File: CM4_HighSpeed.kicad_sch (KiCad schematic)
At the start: 14 parts, among them J12 THD-02-R, J13 1-2199119-5, J14 USB_A, J15 USB_OTG, J16 Conn_01x02, J2 SS-52400-004, J5 690-019-298-412, U11 TPD4EUSB30, U13 RT9742SNGV

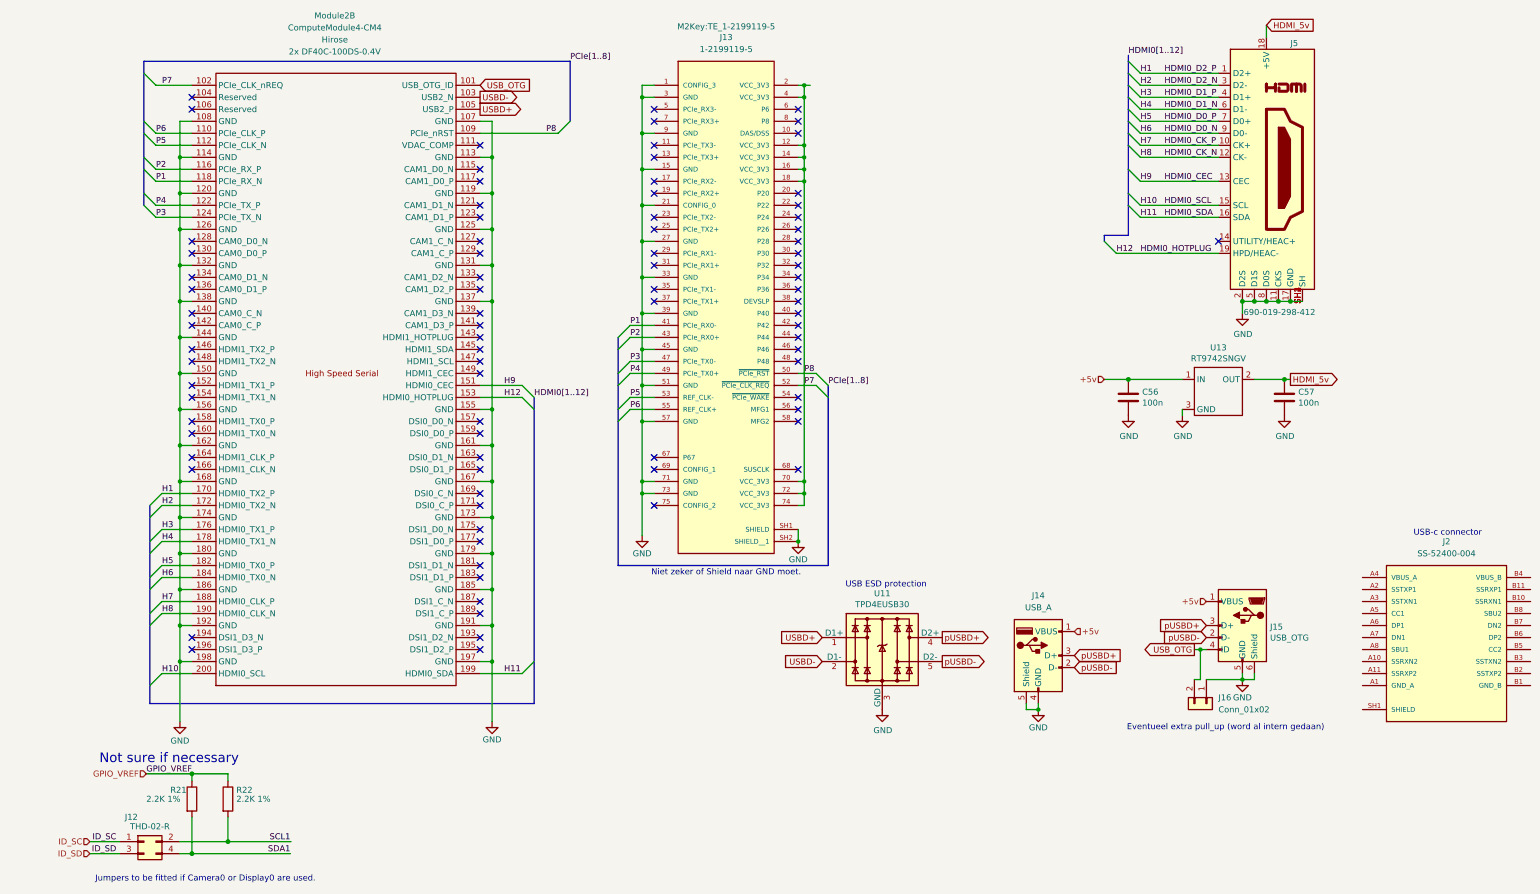
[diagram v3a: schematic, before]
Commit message: Added 3d-models, esd protection, cleaned up and made small start with pcb
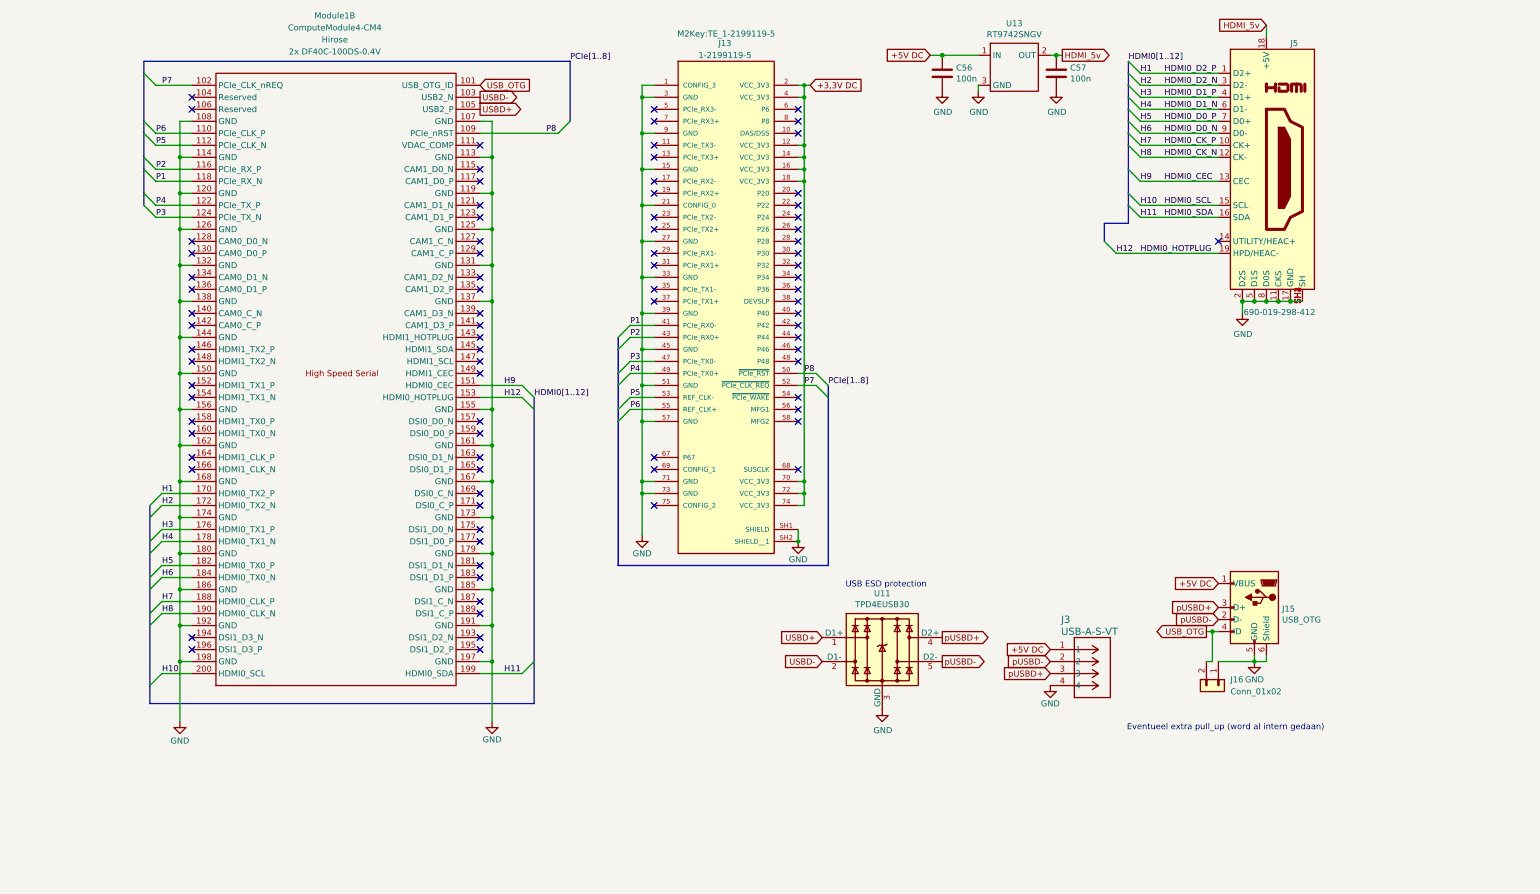
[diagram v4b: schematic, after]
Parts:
- removed J12: THD-02-R, Connector_PinHeader_2.54mm:PinHeader_2x02_P2.54mm_Vertical, symbol Connector_Generic:Conn_02x02_Odd_Even
- removed J14: USB_A, Connector_USB:USB_A_Receptacle_XKB_U231-091N-4BLRA00-S, symbol Connector:USB_A
- removed J2: SS-52400-004, SS-52400-004:STEWART_SS-52400-004 (USB-C), symbol SS-52400-004:SS-52400-004
- removed R21, R22: 2.2K 1%, Resistor_SMD:R_0402_1005Metric, symbol Device:R
- added J3: USB-A-S-VT, USB-A-S-VT:CONN_USB-A-S-VT_ADM, symbol USB-A-S-VT:USB-A-S-VT
- C56, C57: footprint Capacitor_SMD:C_0402_1005Metric -> Capacitor_SMD:C_0603_1608Metric
- J16: footprint (none) -> Connector_PinHeader_2.54mm:PinHeader_1x02_P2.54mm_Vertical
- renumbered Module2 to Module1
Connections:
- net GND: now also J3.4
- net pUSBD+: now also J3.3
- net pUSBD-: now also J3.2
- net +5v renamed +5V DC
- net +5V DC: now also J3.1
- net P7 renamed +3,3V DC
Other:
- note removed: "Jumpers to be fitted if Camera0 or Display0 are used."
- note removed: "Niet zeker of Shield naar GND moet."
- note removed: "Not sure if necessary"
- note removed: "USB-c connector"
- moved on the sheet: C56, C57, J15, J16, U13

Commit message: Adjusted the PCB design, changed footprints to 0402 (temp)
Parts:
- C56, C57: footprint Capacitor_SMD:C_0603_1608Metric -> Capacitor_SMD:C_0402_1005Metric_Pad0.74x0.62mm_HandSolder
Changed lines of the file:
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@@
 			)
 		)
-		(property "Footprint" "Capacitor_SMD:C_0603_1608Metric"
+		(property "Footprint" "Capacitor_SMD:C_0402_1005Metric_Pad0.74x0.62mm_HandSolder"
 			(at 225.7552 29.21 0)
 			(effects
@@
 			)
 		)
-		(property "Footprint" "Capacitor_SMD:C_0603_1608Metric"
+		(property "Footprint" "Capacitor_SMD:C_0402_1005Metric_Pad0.74x0.62mm_HandSolder"
 			(at 201.6252 29.21 0)
 			(effects

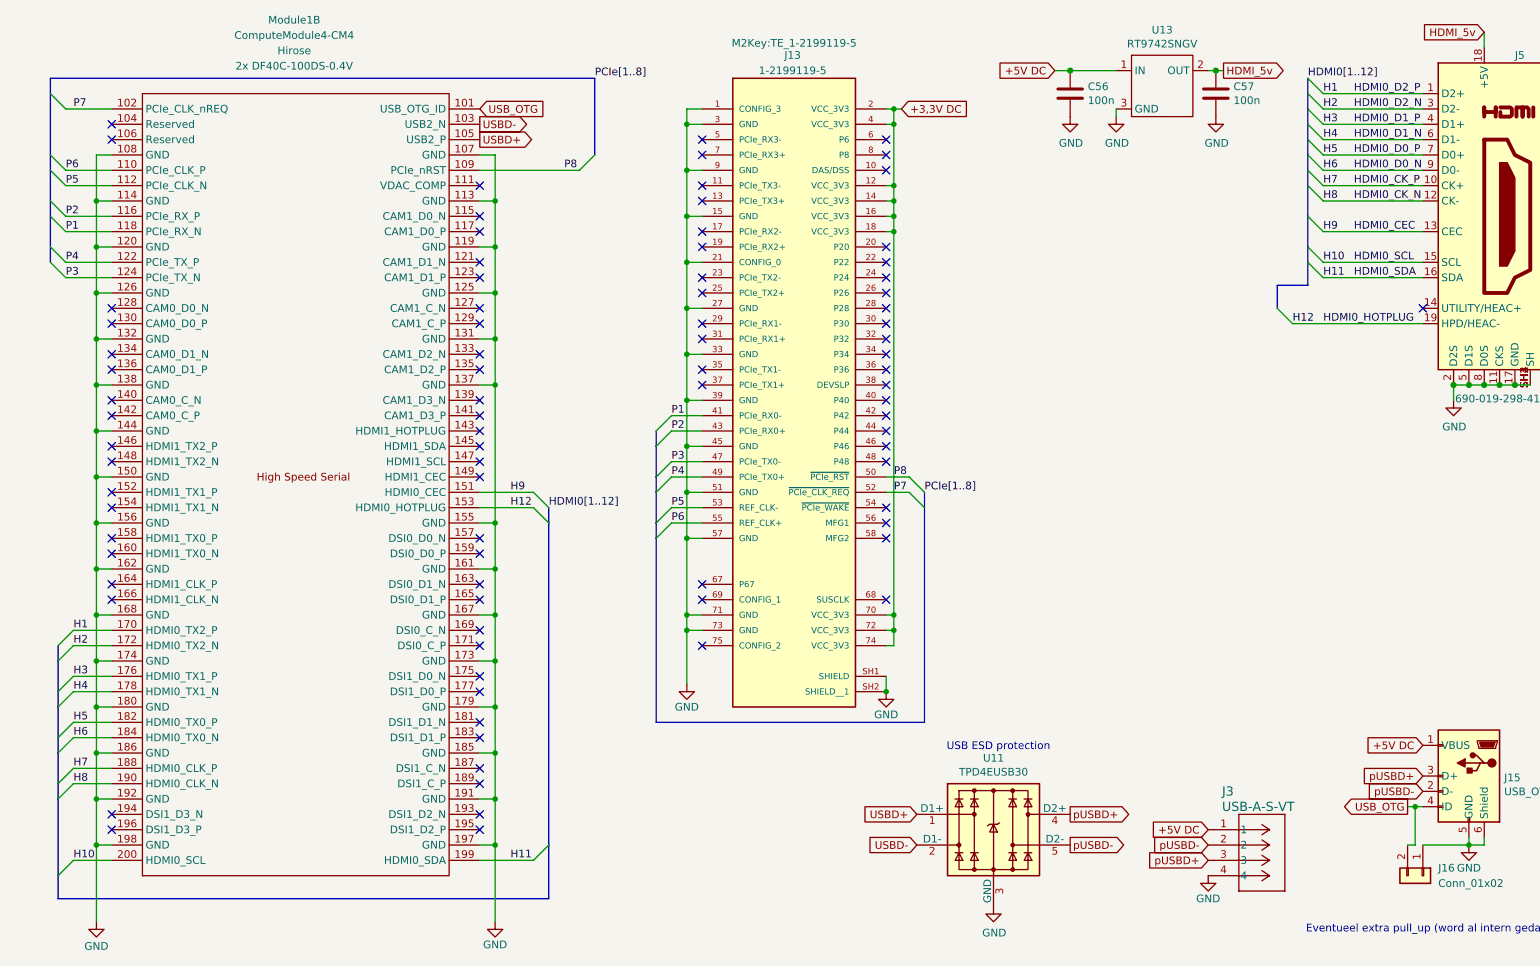
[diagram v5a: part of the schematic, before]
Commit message: Adjusted netclasses to route differential pairs for PCIe and HDMI. And used JLCPCB to adjust trace width for those
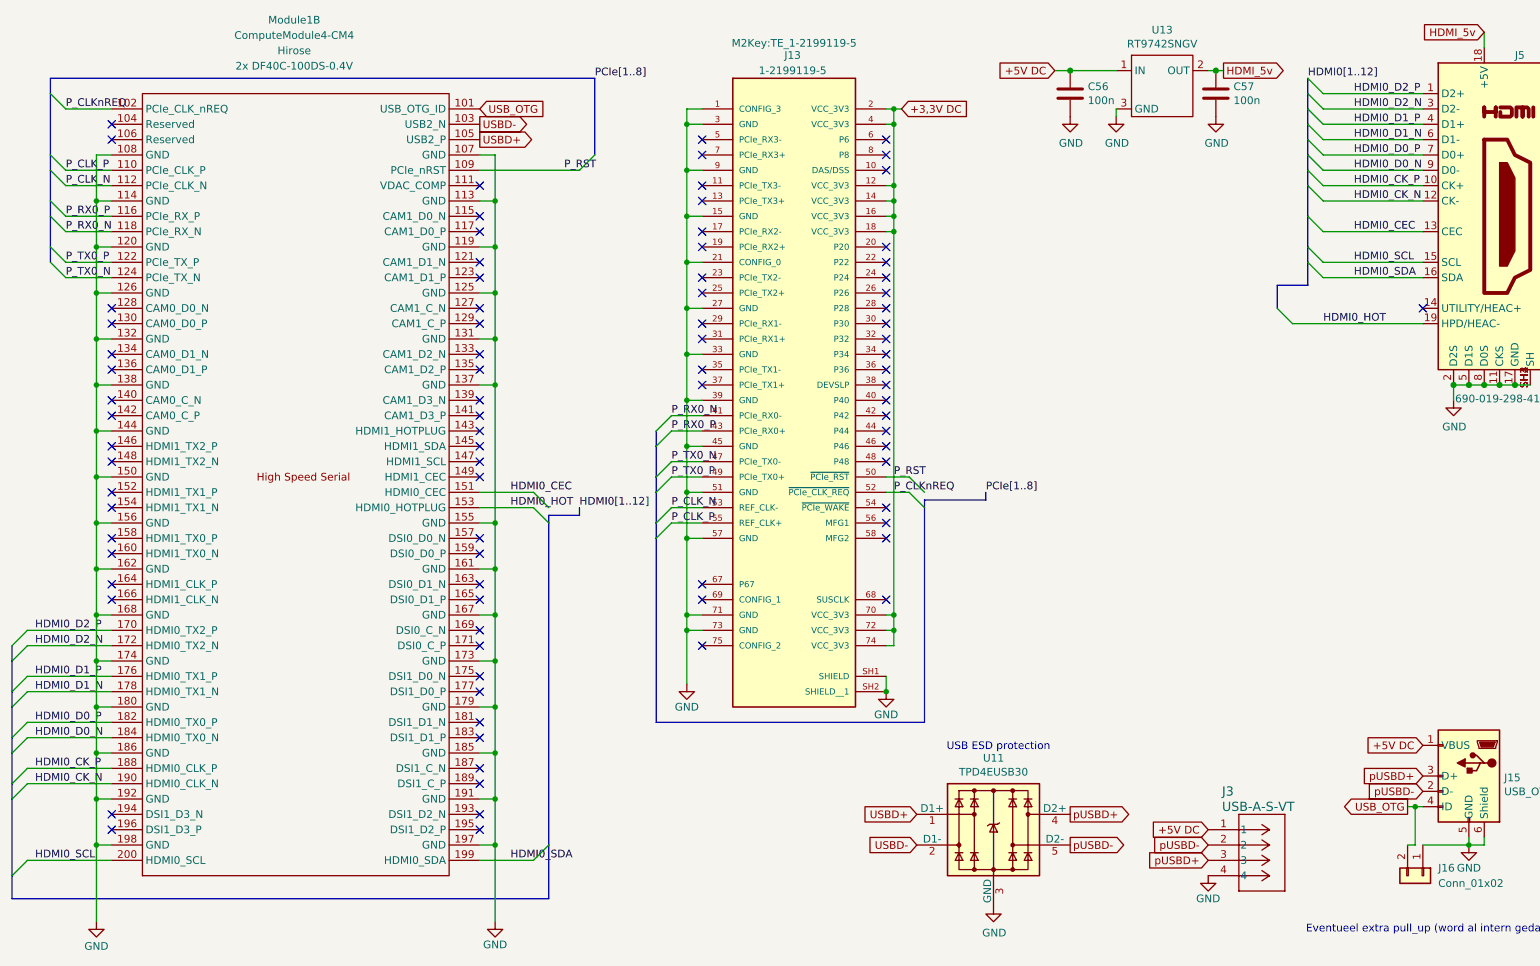
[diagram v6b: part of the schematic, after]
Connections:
- net H1 renamed HDMI0_D2_P
- net H10 renamed HDMI0_SCL
- net H11 renamed HDMI0_SDA
- net H12 renamed HDMI0_HOT
- net H2 renamed HDMI0_D2_N
- net H3 renamed HDMI0_D1_P
- net H4 renamed HDMI0_D1_N
- net H5 renamed HDMI0_D0_P
- net H6 renamed HDMI0_D0_N
- net H7 renamed HDMI0_CK_P
- net H8 renamed HDMI0_CK_N
- net H9 renamed HDMI0_CEC
- net P1 renamed P_RX0_N
- net P2 renamed P_RX0_P
- net P3 renamed P_TX0_N
- net P4 renamed P_TX0_P
- net P5 renamed P_CLK_N
- net P6 renamed P_CLK_P

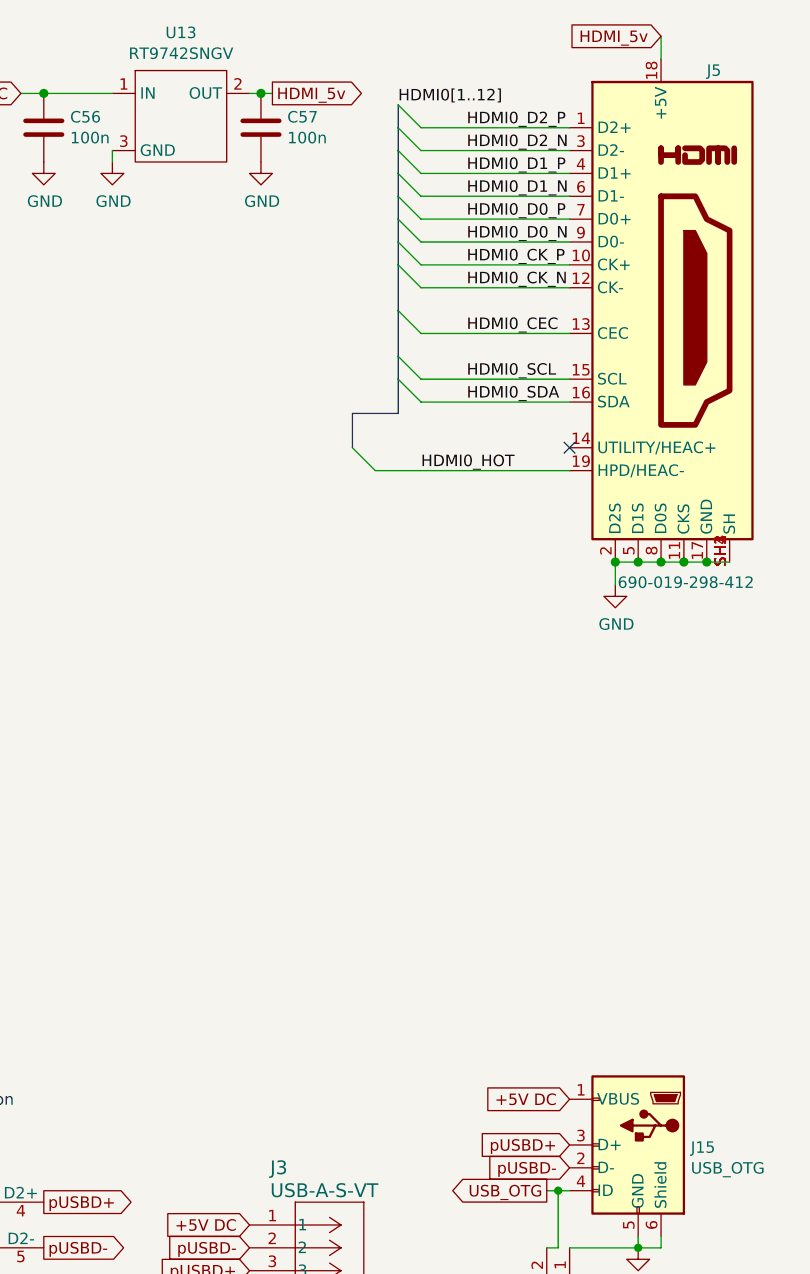
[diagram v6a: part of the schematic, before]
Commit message: heb de GPIO aangepast.
Laten we morgen de stand van zaken bespreken. En overleggen wat we kunnen doen
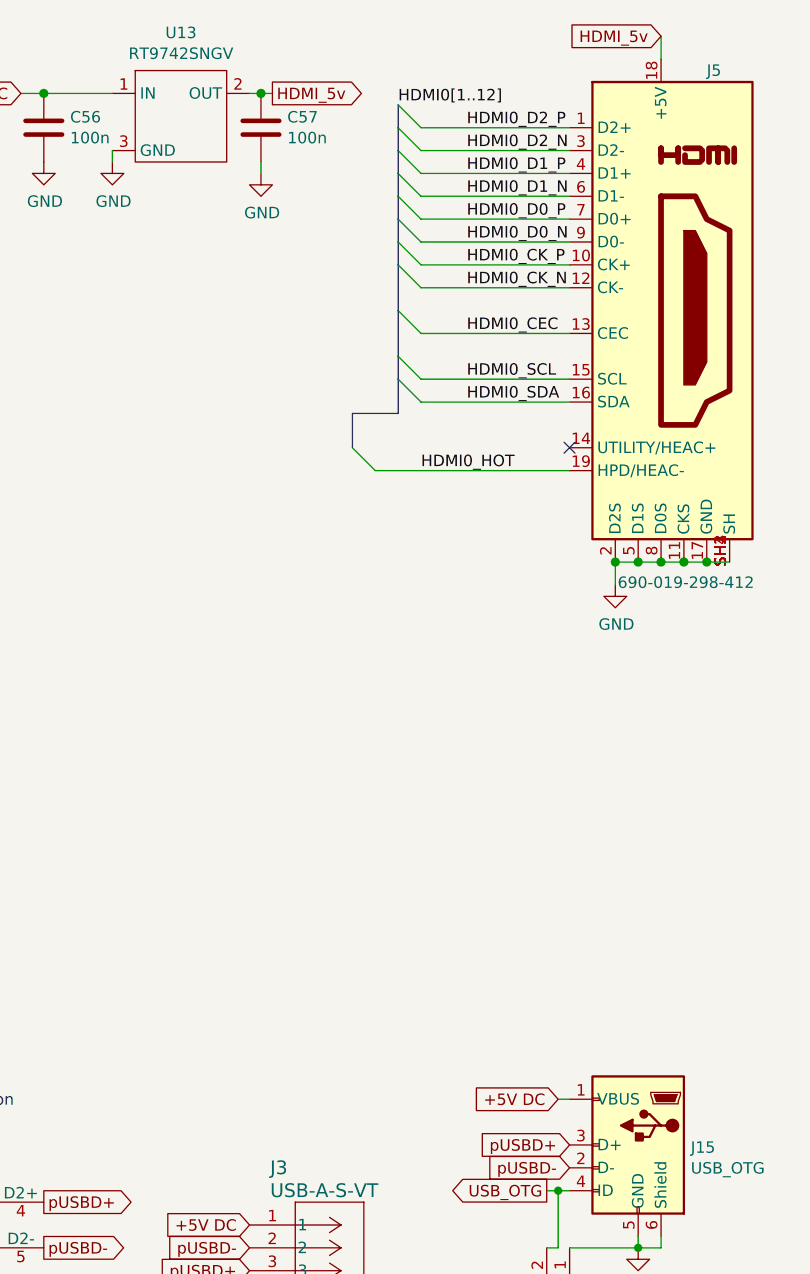
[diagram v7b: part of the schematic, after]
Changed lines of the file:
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@@
 	(wire
 		(pts
+			(xy 224.79 30.48) (xy 224.79 29.21)
+		)
+		(stroke
+			(width 0)
+			(type default)
+		)
+	)
+	(wire
+		(pts
 			(xy 264.16 73.66) (xy 264.16 76.2)
 		)
@@
 	(wire
 		(pts
+			(xy 257.81 133.35) (xy 259.08 133.35)
+		)
+		(stroke
+			(width 0)
+			(type default)
+		)
+	)
+	(wire
+		(pts
 			(xy 102.87 142.24) (xy 105.41 142.24)
 		)
@@
 	(global_label "+5V DC"
 		(shape input)
-		(at 259.08 133.35 180)
+		(at 257.81 133.35 180)
 		(fields_autoplaced yes)
 		(effects
@@
 		)
 		(property "Intersheetrefs" "${INTERSHEET_REFS}"
-			(at 248.7167 133.35 0)
+			(at 247.4467 133.35 0)
 			(effects
 				(font
@@
 	(symbol
 		(lib_id "power:GND")
-		(at 224.79 29.21 0)
+		(at 224.79 30.48 0)
 		(unit 1)
 		(exclude_from_sim no)
@@
 		(dnp no)
 		(property "Reference" "#PWR05"
-			(at 224.79 35.56 0)
+			(at 224.79 36.83 0)
 			(effects
 				(font
@@
 		)
 		(property "Value" "GND"
-			(at 224.917 33.6042 0)
+			(at 224.917 34.8742 0)
 			(effects
 				(font
@@
 		)
 		(property "Footprint" ""
-			(at 224.79 29.21 0)
+			(at 224.79 30.48 0)
 			(effects
 				(font
@@
 		)
 		(property "Datasheet" ""
-			(at 224.79 29.21 0)
+			(at 224.79 30.48 0)
 			(effects
 				(font
@@
 		)
 		(property "Description" ""
-			(at 224.79 29.21 0)
+			(at 224.79 30.48 0)
 			(effects
 				(font

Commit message: Added lots and lots of traces in PCB design.
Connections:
- net +3,3V DC: no longer J13.50 (~{PCIe_RST}), J13.52 (~{PCIe_CLK_REQ}), Module1.102 (PCIe_CLK_nREQ), Module1.109 (PCIe_nRST)
- new net P_CLKnREQ: J13.52 (~{PCIe_CLK_REQ}), Module1.102 (PCIe_CLK_nREQ)
- new net P_RST: J13.50 (~{PCIe_RST}), Module1.109 (PCIe_nRST)
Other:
- moved on the sheet: J13, J15, J16, J3
